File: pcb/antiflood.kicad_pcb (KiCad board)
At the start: 2 copper layers, 92 x 74 mm, 71 parts, among them J1 Barrel_Jack, J10 Screw_Terminal_01x02, J11 Screw_Terminal_01x02, J12 Screw_Terminal_01x02, J13 Screw_Terminal_01x02, J14 Screw_Terminal_01x02, J15 Screw_Terminal_01x02, J16 GS2, J2 Conn_01x04, J4 Conn_02x04_Odd_Even, J5 01x03, J7 01x03, J8 Conn_02x03_Odd_Even, J9 Conn_01x07, K1 P-5, K2 P-5, Q1 2N3904, Q2 2N3904, SW1 SW_Push, SW2 SW_Push, SW3 SW_Push, U1 ATMEGA328P-AU, U2 LM7812_TO220, U3 LM7805_TO220, U4 LM1117-3.3, Y1 16MHz

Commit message: Update.
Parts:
- removed ? (x4): MountingHole_2.5mm_Pad, Mounting_Holes:MountingHole_2.5mm_Pad
- removed J14, J15: Screw_Terminal_01x02, Connectors_Terminal_Blocks:TerminalBlock_bornier-2_P5.08mm
- removed J16: GS2, Connectors:GS2
- removed JP1: Jumper_NC_Dual, Pin_Headers:Pin_Header_Straight_1x03_Pitch2.54mm
- added C11: 22p, Capacitors_SMD:C_1206, F.Cu at (134.0, 95.9)
- added C12: 22p, Capacitors_SMD:C_1206, F.Cu at (153.0, 95.9)
- added D10: LED, LEDs:LED_1206, F.Cu at (159.4, 92.1)
- added D11: LED, LEDs:LED_1206, F.Cu at (159.4, 97.2)
- added D12: LED, LEDs:LED_1206, F.Cu at (159.4, 99.7)
- added D9: LED, LEDs:LED_1206, F.Cu at (159.4, 94.6)
- added J3: 01x03, Connectors_Terminal_Blocks:TerminalBlock_bornier-3_P5.08mm, F.Cu at (170.8, 90.8)
- added J6: Conn_02x05_Odd_Even, Socket_Strips:Socket_Strip_Straight_2x05_Pitch2.54mm, F.Cu at (132.7, 109.9)
- added L1: 170, Inductors_SMD:L_12x12mm_h6mm, F.Cu at (112.4, 79.4)
- added L2: 220, Inductors_SMD:L_12x12mm_h6mm, F.Cu at (112.4, 93.3)
- added R23: 3k3, Resistors_SMD:R_0805, F.Cu at (145.4, 112.4)
- added R24: 3k3, Resistors_SMD:R_0805, F.Cu at (145.4, 104.8)
- added R25: 3k3, Resistors_SMD:R_0805, F.Cu at (141.6, 112.4)
- added R26: 1k, Resistors_SMD:R_0805, F.Cu at (141.6, 108.6)
- added R27: 1k, Resistors_SMD:R_0805, F.Cu at (141.6, 104.8)
- added R28: 1k, Resistors_SMD:R_0805, F.Cu at (137.8, 112.4)
- added R29: 1k, Resistors_SMD:R_0805, F.Cu at (137.8, 104.8)
- added R30: 1k, Resistors_SMD:R_0805, F.Cu at (137.8, 108.6)
- added R31: 1k, Resistors_SMD:R_0805, F.Cu at (153.0, 102.2)
- added R32: 1M, Resistors_SMD:R_0805, F.Cu at (149.2, 102.2)
- added U5: MC34063, SMD_Packages:SOIC-8-N, F.Cu at (113.7, 114.9)
- added U6: TP4056, SMD_Packages:SOIC-8-N, F.Cu at (101.0, 114.9)
- C1, C5: value 0.1 -> 100; footprint Capacitors_SMD:C_1206 -> Capacitors_SMD:CP_Elec_6.3x5.7
- C10: value 22p -> 0.1
- C2, C4: value 100 -> 0.1; footprint Capacitors_SMD:CP_Elec_6.3x5.7 -> Capacitors_SMD:C_1206
- C3: value 47 -> 470
- C6: value 47 -> 0.1; footprint Capacitors_SMD:CP_Elec_6.3x5.7 -> Capacitors_SMD:C_1206
- C7: value 0.1 -> 470p
- C8: value 0.1 -> 1n5
- C9: value 22p -> 100; footprint Capacitors_SMD:C_1206 -> Capacitors_SMD:CP_Elec_6.3x5.7
- D5, D6: value LED -> D; footprint LEDs:LED_1206 -> Diodes_SMD:D_SMA
- J2: value Conn_01x04 -> 01x03; footprint Socket_Strips:Socket_Strip_Straight_1x04_Pitch2.54mm -> Connectors_Terminal_Blocks:TerminalBlock_bornier-3_P5.08mm
- J4: value Conn_02x04_Odd_Even -> Conn_02x05_Odd_Even; footprint Socket_Strips:Socket_Strip_Straight_2x04_Pitch2.54mm -> Socket_Strips:Socket_Strip_Straight_2x05_Pitch2.54mm
- J5: value 01x03 -> Conn_02x04_Odd_Even; footprint Connectors_Terminal_Blocks:TerminalBlock_bornier-3_P5.08mm -> Socket_Strips:Socket_Strip_Straight_2x04_Pitch2.54mm
- J7: value 01x03 -> Conn_02x03_Odd_Even; footprint Connectors_Terminal_Blocks:TerminalBlock_bornier-3_P5.08mm -> Socket_Strips:Socket_Strip_Straight_2x03_Pitch2.54mm
- J8: value Conn_02x03_Odd_Even -> Screw_Terminal_01x02; footprint Pin_Headers:Pin_Header_Straight_2x03_Pitch2.54mm -> Connectors_Terminal_Blocks:TerminalBlock_bornier-2_P5.08mm
- J9: value Conn_01x07 -> Screw_Terminal_01x02; footprint Socket_Strips:Socket_Strip_Straight_1x07_Pitch2.54mm -> Connectors_Terminal_Blocks:TerminalBlock_bornier-2_P5.08mm
- R1: value 82 -> 1k5
- R10: value 33k -> 1k2
- R11: value 33k -> 180
- R12: value 3k3 -> 3k6
- R13: value 0.5 -> 3k6; footprint Resistors_SMD:R_2010 -> Resistors_SMD:R_0805
- R15: value 3k3 -> 0.5; footprint Resistors_SMD:R_0805 -> Resistors_SMD:R_2010
- R16: value 1M -> R
- R17: value 100 -> 10k
- R18: value 100 -> R
- R19, R22: value 100 -> 1k5
- R20, R21: value 100 -> 3k3
- R4: value 1k5 -> 82
- R5: value 3k3 -> 1k
- R6: value 3k3 -> 0.22
- R7: value 3k3 -> 0.33
- R8: value 1k5 -> 1k
- R9: value 3k3 -> 1k2
- SW1, SW2, SW3: footprint Buttons_Switches_THT:SW_Tactile_SPST_Angled_PTS645Vx83-2LFS -> Buttons_Switches_SMD:SW_SPST_SKQG
- U1: value ATMEGA328P-AU -> LM1117-3.3; footprint Housings_QFP:TQFP-32_7x7mm_Pitch0.8mm -> TO_SOT_Packages_SMD:SOT-223-3_TabPin2
- U2: value LM7812_TO220 -> ATMEGA328P-AU; footprint TO_SOT_Packages_THT:TO-220-3_Horizontal -> Housings_QFP:TQFP-32_7x7mm_Pitch0.8mm
- U4: value LM1117-3.3 -> MC34063; footprint TO_SOT_Packages_SMD:SOT-223-3_TabPin2 -> SMD_Packages:SOIC-8-N
- moved J13 116.9 mm to (236.9, 121.3)
- moved J12 100.7 mm to (226.7, 121.3)
- moved J11 86.2 mm to (216.5, 121.3)
- moved D6 85.2 mm to (98.4, 101.0), turned to 0 degrees
- moved D5 84.1 mm to (98.4, 95.9), turned to 0 degrees
- moved SW2 80.3 mm to (197.5, 80.6), turned to 0 degrees
- moved J10 74.5 mm to (206.4, 121.3)
- moved R12 69.5 mm to (164.5, 106.0), turned to 0 degrees
- moved R7 68.5 mm to (156.8, 117.5), turned to 0 degrees
- moved U1 67.4 mm to (108.6, 106.0)
- moved R6 64.5 mm to (156.8, 113.7), turned to 0 degrees
- moved R9 62.5 mm to (160.7, 106.0), turned to 0 degrees
- moved C9 60.5 mm to (99.7, 76.8)
- moved D1 59.5 mm to (98.4, 90.8)
- moved R5 57.9 mm to (156.8, 106.0)
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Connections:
- C1 pad 1: Net-(C1-Pad1) -> +12V
- C10 pad 1: /O2 -> /RST
- C2 pad 1: Net-(C1-Pad1) -> +12V
- C3 pad 1: +12V -> +5V
- C5 pad 1: GND -> +3V3
- C5 pad 2: +5V -> GND
- C7 pad 1: +3V3 -> Net-(C7-Pad1)
- C8 pad 1: /RST -> Net-(C8-Pad1)
- C9 pad 1: /O1 -> /BAT
- D1 pad 2: /FON -> Net-(D1-Pad2)
- D2 pad 2: /FCL -> Net-(D2-Pad2)
- D4 pad 1: Net-(D3-Pad1) -> Net-(D4-Pad1)
- D5 pad 1: Net-(D3-Pad1) -> +12V
- D6 pad 1: Net-(D3-Pad1) -> Net-(D6-Pad1)
- D6 pad 2: Net-(D6-Pad2) -> GND
- D7 pad 1: Net-(D3-Pad1) -> GND
- D8 pad 1: Net-(D3-Pad1) -> GND
- J1 pad 1: Net-(C1-Pad1) -> +12V
- J10 pad 2: /A0 -> /A2
- J11 pad 2: /A1 -> /A3
- J12 pad 2: /A2 -> /A4
- J13 pad 2: /A3 -> /A5
- J2 pad 1: GND -> Net-(J2-Pad1)
- J2 pad 2: +5V -> /A6
- J4 pad 2: /WRX -> GND
- J4 pad 3: Net-(J4-Pad3) -> /BAT
- J4 pad 4: Net-(J4-Pad4) -> /BTMP
- J4 pad 5: Net-(J4-Pad5) -> /BAT
- J4 pad 6: Net-(J4-Pad6) -> /BTMP
- J4 pad 7: Net-(J4-Pad7) -> +12V
- J4 pad 8: +3V3 -> +5V
- J5 pad 1: Net-(J5-Pad1) -> GND
- J5 pad 2: /A6 -> /WRX
- J7 pad 1: Net-(J7-Pad1) -> /L4
- J7 pad 2: /A6 -> +5V
- J7 pad 3: Net-(J7-Pad3) -> /L5
- J8 pad 2: /RST -> /A0
- J9 pad 2: /L5 -> /A1
- K1 pad 10: /FON -> Net-(D1-Pad2)
- K1 pad 3: Net-(J5-Pad1) -> Net-(J2-Pad1)
- K1 pad 4: VDDA -> +12V
- K1 pad 7: VDDA -> +12V
- K1 pad 8: Net-(J7-Pad1) -> Net-(J3-Pad1)
- K2 pad 10: /FCL -> Net-(D2-Pad2)
- K2 pad 3: Net-(J5-Pad3) -> Net-(J2-Pad3)
- K2 pad 4: VDDA -> +12V
- K2 pad 7: VDDA -> +12V
- K2 pad 8: Net-(J7-Pad3) -> Net-(J3-Pad3)
- Q1 pad 3: /FON -> Net-(D1-Pad2)
- Q2 pad 3: /FCL -> Net-(D2-Pad2)
- R1 pad 1: Net-(R1-Pad1) -> Net-(D1-Pad2)
- R1 pad 2: Net-(Q1-Pad2) -> /FON
- R10 pad 1: /FON -> Net-(R10-Pad1)
- R10 pad 2: /A7 -> GND
- R11 pad 1: /A7 -> Net-(L1-Pad1)
- R11 pad 2: /FCL -> Net-(R11-Pad2)
- R12 pad 1: Net-(J4-Pad7) -> +5V
- R12 pad 2: GND -> Net-(R12-Pad2)
- R13 pad 1: GND -> +12V
- R13 pad 2: /A6 -> Net-(R10-Pad1)
- R14 pad 1: GND -> /A6
- R14 pad 2: /A6 -> GND
- R15 pad 1: +5V -> /A6
- R15 pad 2: /RST -> GND
- R16 pad 1: /O1 -> /BTMP
- R16 pad 2: /O2 -> +5V
- R17 pad 1: Net-(D3-Pad2) -> Net-(R17-Pad1)
- R17 pad 2: /L0 -> GND
- R18 pad 1: Net-(D4-Pad2) -> /BTMP
- R18 pad 2: /L1 -> GND
- R19 pad 1: Net-(D5-Pad2) -> Net-(J5-Pad4)
- R19 pad 2: /L2 -> /WCC
- R2 pad 1: Net-(R2-Pad1) -> /PON
- R2 pad 2: Net-(Q2-Pad2) -> Net-(Q1-Pad2)
- R20 pad 1: Net-(D6-Pad2) -> Net-(J5-Pad4)
- R20 pad 2: /L3 -> GND
- R21 pad 1: Net-(D7-Pad2) -> Net-(J5-Pad5)
- R21 pad 2: /L4 -> +3V3
- R22 pad 1: Net-(D8-Pad2) -> Net-(J5-Pad7)
- R22 pad 2: /L5 -> /WTX
- R3 pad 1: Net-(J4-Pad4) -> Net-(D2-Pad2)
- R3 pad 2: /WCE -> /FCL
- R4 pad 1: Net-(J4-Pad6) -> Net-(Q2-Pad2)
- R4 pad 2: /WCR -> /PCL
- R5 pad 1: GND -> +5V
- R5 pad 2: Net-(J4-Pad4) -> Net-(D3-Pad2)
- R6 pad 1: Net-(J4-Pad6) -> Net-(L1-Pad1)
- R6 pad 2: GND -> /BAT
- R7 pad 1: Net-(J4-Pad5) -> Net-(R7-Pad1)
- R7 pad 2: +3V3 -> +12V
- R8 pad 1: Net-(J4-Pad7) -> +5V
- R8 pad 2: /WTX -> Net-(D4-Pad2)
- R9 pad 1: Net-(J4-Pad3) -> Net-(R12-Pad2)
- R9 pad 2: +3V3 -> GND
- SW1 pad 1: /FON -> Net-(D1-Pad2)
- SW2 pad 1: /FCL -> Net-(D2-Pad2)
- U1 pad 1: /WCR -> GND
- U1 pad 2: Net-(J2-Pad4) -> +5V
- U1 pad 3: GND -> +12V
- U2 pad 1: Net-(C1-Pad1) -> /CHG
- U2 pad 2: GND -> /FON
- U2 pad 3: +12V -> GND
- U3 pad 1: +12V -> +5V
- U3 pad 3: +5V -> +3V3
- U4 pad 1: GND -> Net-(R7-Pad1)
- U4 pad 2: +3V3 -> Net-(D6-Pad1)
- U4 pad 3: +5V -> Net-(C7-Pad1)
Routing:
- net +5V: track 224.7 -> 0.00 mm, vias 5 -> 0
- net GND: track 180.6 -> 0.00 mm, vias 23 -> 0
- net /A6: track 132.7 -> 0.00 mm, vias 2 -> 0
- net /A7: track 113.2 -> 0.00 mm, vias 3 -> 0
- net /WRX: track 67.3 -> 0.00 mm, vias 2 -> 0
- net +12V: track 65.7 -> 0.00 mm
- net /L5: track 64.0 -> 0.00 mm
- net /A5: track 61.9 -> 0.00 mm
- net /WCE: track 59.9 -> 0.00 mm
- net /L3: track 58.1 -> 0.00 mm
- net /L4: track 56.6 -> 0.00 mm
- net /WTX: track 55.7 -> 0.00 mm
- net VDDA: track 55.2 -> 0.00 mm
- net +3V3: track 54.2 -> 0.00 mm
- net /RST: track 54.1 -> 0.00 mm, vias 1 -> 0
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- removed copper zone on B.Cu, net GND
- removed copper zone on F.Cu, net GND
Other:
- board outline removed
- board text removed: "12V"
- board text removed: "5V"
- board text removed: "ANTIFLOOD PROJECT BETA 174:DBAC3ABEB3F1"
- board text removed: "Copyright 17 sep 2018 Alexey <Inverse> Shumeiko"
- board text removed: "ESP01"
- board text removed: "ICSP"
- board text removed: "Valve Control Module"
- board text removed: "dbg"
- board text removed: "λ"

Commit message: PCB: add borders
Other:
- board outline added: 88 x 84 mm
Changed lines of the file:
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@@
     (links 207)
     (no_connects 207)
-    (area 0 0 0 0)
+    (area 94.699999 62.74 248.023573 136.12)
     (thickness 1.6)
-    (drawings 0)
+    (drawings 21)
     (tracks 0)
     (zones 0)
@@
   (layers
     (0 F.Cu signal)
-    (31 B.Cu signal hide)
+    (31 B.Cu signal)
     (32 B.Adhes user)
     (33 F.Adhes user)
@@
     (pad_drill 1.3)
     (pad_to_mask_clearance 0)
-    (aux_axis_origin 103.505 53.975)
-    (grid_origin 103.505 53.975)
-    (visible_elements FFFEF77F)
+    (aux_axis_origin 71.505 50.975)
+    (grid_origin 71.505 50.975)
+    (visible_elements FFFE317F)
     (pcbplotparams
       (layerselection 0x00030_80000001)
@@
     )
   )
+  (gr_line (start 158.505 57.975) (end 72.505 57.975) (angle 90) (layer Eco1.User) (width 0.2))
+  (gr_line (start 158.505 127.975) (end 72.505 127.975) (angle 90) (layer Eco1.User) (width 0.2))
+  (gr_line (start 76.505 67.975) (end 80.505 67.975) (angle 90) (layer Eco2.User) (width 0.2))
+  (gr_line (start 78.505 69.975) (end 78.505 65.975) (angle 90) (layer Eco2.User) (width 0.2))
+  (gr_line (start 76.505 117.975) (end 80.505 117.975) (angle 90) (layer Eco2.User) (width 0.2))
+  (gr_line (start 78.505 115.975) (end 78.505 119.975) (angle 90) (layer Eco2.User) (width 0.2))
+  (gr_line (start 153.505 67.975) (end 149.505 67.975) (angle 90) (layer Eco2.User) (width 0.2))
+  (gr_line (start 151.505 69.975) (end 151.505 65.975) (angle 90) (layer Eco2.User) (width 0.2))
+  (gr_line (start 151.505 115.975) (end 151.505 119.975) (angle 90) (layer Eco2.User) (width 0.2))
+  (gr_line (start 149.505 117.975) (end 153.505 117.975) (angle 90) (layer Eco2.User) (width 0.2))
+  (gr_line (start 105.505 136.975) (end 105.505 135.975) (angle 90) (layer Eco1.User) (width 0.2))
+  (gr_line (start 105.505 112.975) (end 105.505 135.975) (angle 90) (layer Eco1.User) (width 0.2))
+  (gr_line (start 125.505 112.975) (end 125.505 136.975) (angle 90) (layer Eco1.User) (width 0.2))
+  (gr_line (start 161.505 112.975) (end 69.505 112.975) (angle 90) (layer Eco1.User) (width 0.2))
+  (gr_line (start 69.505 72.975) (end 161.505 72.975) (angle 90) (layer Eco1.User) (width 0.2))
+  (gr_line (start 115.505 48.975) (end 115.505 136.975) (angle 90) (layer Eco2.User) (width 0.2))
+  (gr_line (start 69.505 92.975) (end 161.505 92.975) (angle 90) (layer Eco2.User) (width 0.2))
+  (gr_line (start 71.505 134.975) (end 71.505 50.975) (angle 90) (layer Edge.Cuts) (width 0.1))
+  (gr_line (start 159.505 134.975) (end 71.505 134.975) (angle 90) (layer Edge.Cuts) (width 0.1))
+  (gr_line (start 159.505 50.975) (end 159.505 134.975) (angle 90) (layer Edge.Cuts) (width 0.1))
+  (gr_line (start 71.505 50.975) (end 159.505 50.975) (angle 90) (layer Edge.Cuts) (width 0.1))
 )

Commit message: PCB: pre placement of lements
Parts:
- moved J8 130.0 mm to (74.3, 55.0)
- moved J9 129.7 mm to (84.8, 55.0)
- moved J10 129.4 mm to (95.3, 55.0)
- moved J11 129.1 mm to (105.8, 55.0)
- moved J12 128.8 mm to (116.3, 55.0)
- moved J13 128.5 mm to (126.8, 55.0)
- moved SW1 123.5 mm to (76.1, 131.5)
- moved SW2 117.0 mm to (92.1, 131.5)
- moved SW3 117.0 mm to (101.0, 131.5)
- moved D11 85.0 mm to (81.7, 131.5), turned to 90 degrees
- moved D12 81.6 mm to (84.2, 131.5), turned to 90 degrees
- moved C12 74.7 mm to (83.7, 123.6), turned to 90 degrees
- moved J5 64.3 mm to (76.3, 83.2), turned to 90 degrees
- moved R1 58.2 mm to (209.0, 101.5)
- moved R10 58.2 mm to (216.7, 93.9)
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
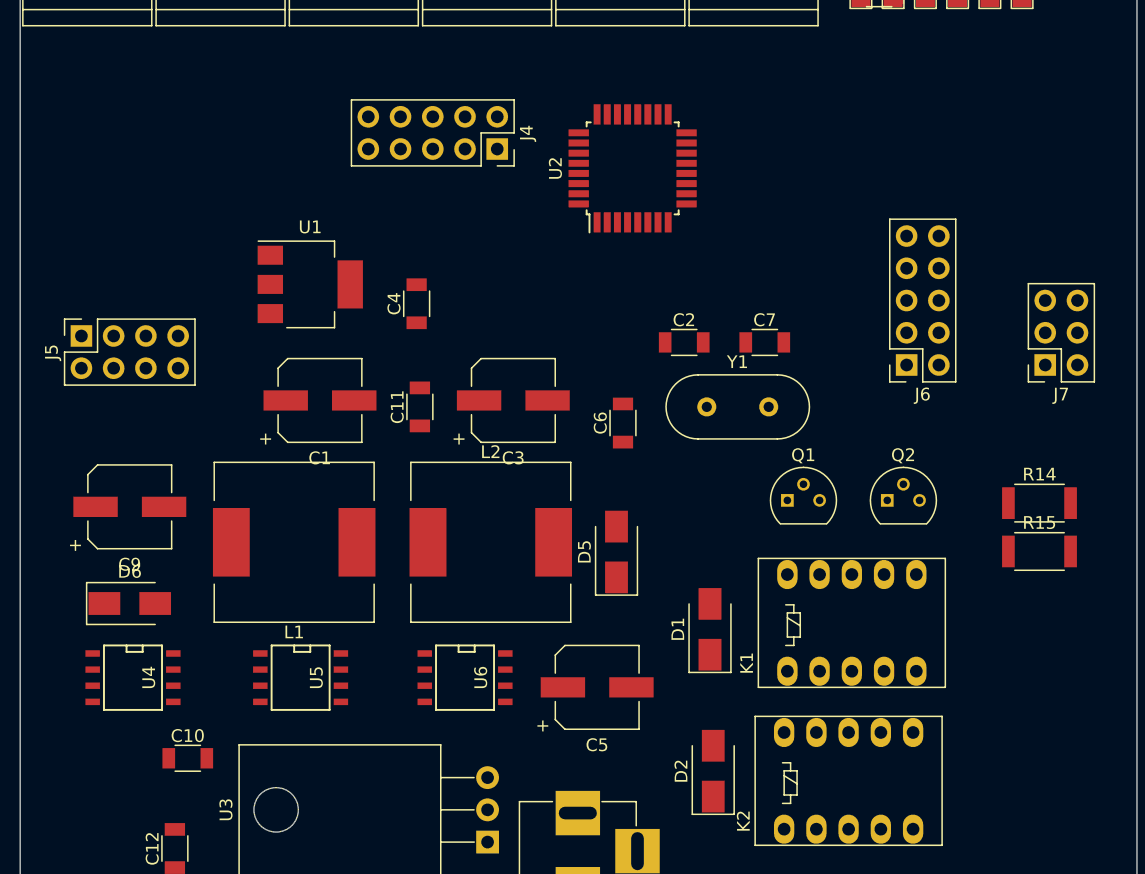
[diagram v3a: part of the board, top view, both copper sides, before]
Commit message: Schematics: rework power lines
1. Replace MC34063 with MT3608, which has a plain EN-pin.
2. Automatic controls on booster and charger.
3. CPU awarness about external power presence.
4. CPU awarness of battery voltage.
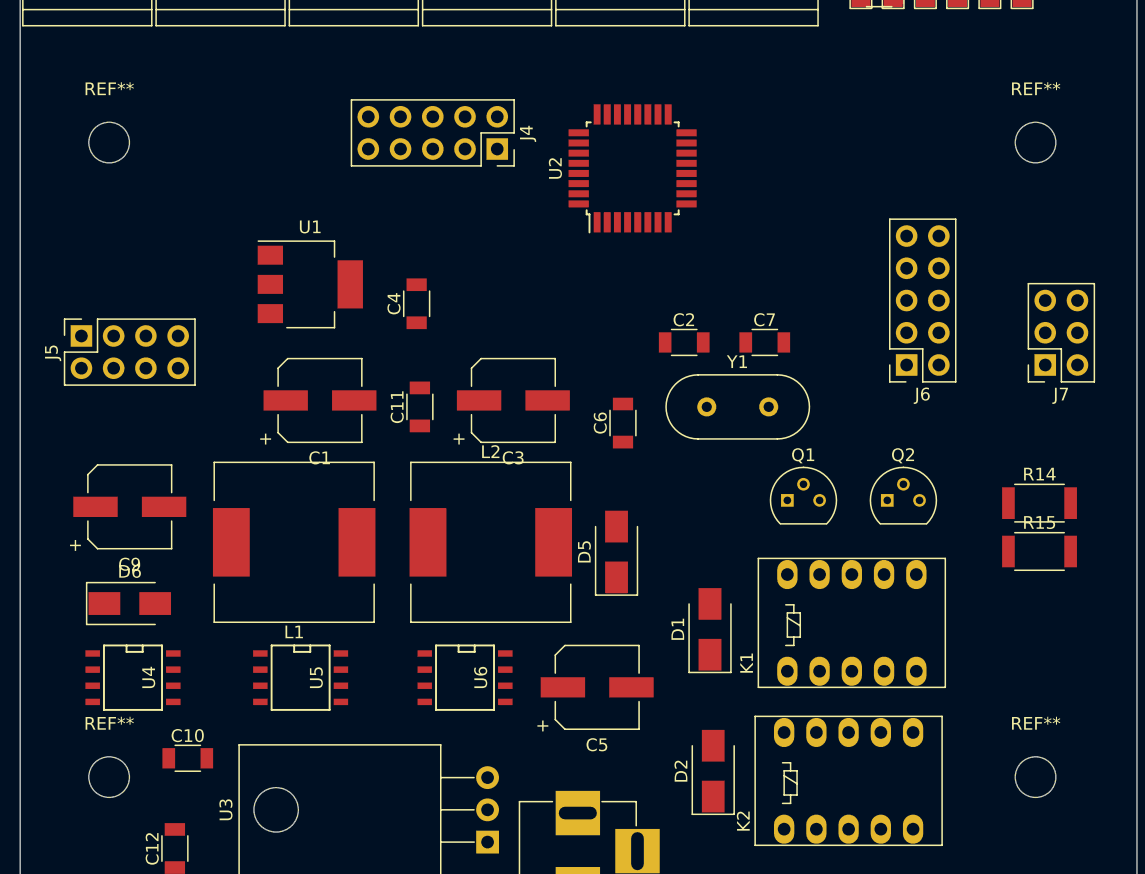
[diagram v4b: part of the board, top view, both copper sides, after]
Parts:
- added REF**: MountingHole_3.2mm_M3, Mounting_Holes:MountingHole_3.2mm_M3, F.Cu at (151.5, 118.0)
- added REF**: MountingHole_3.2mm_M3, Mounting_Holes:MountingHole_3.2mm_M3, F.Cu at (78.5, 118.0)
- added REF**: MountingHole_3.2mm_M3, Mounting_Holes:MountingHole_3.2mm_M3, F.Cu at (78.5, 68.0)
- added REF**: MountingHole_3.2mm_M3, Mounting_Holes:MountingHole_3.2mm_M3, F.Cu at (151.5, 68.0)
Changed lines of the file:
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@@
     (links 207)
     (no_connects 207)
-    (area 71.454999 50.924999 159.555001 135.025001)
+    (area 2.046999 48.874999 222.240001 137.075001)
     (thickness 1.6)
     (drawings 21)
     (tracks 0)
     (zones 0)
-    (modules 85)
+    (modules 89)
     (nets 64)
   )
@@
     (add_net "Net-(R7-Pad1)")
   )
+  (module Mounting_Holes:MountingHole_3.2mm_M3 (layer F.Cu)
+    (at 151.515 117.993)
+    (descr "Mounting Hole 3.2mm, no annular, M3")
+    (tags "mounting hole 3.2mm no annular m3")
+    (attr virtual)
+    (fp_text reference REF** (at 0 -4.2) (layer F.SilkS)
+      (effects (font (size 1 1) (thickness 0.15)))
+    )
+    (fp_text value MountingHole_3.2mm_M3 (at 0 4.2) (layer F.Fab)
+      (effects (font (size 1 1) (thickness 0.15)))
+    )
+    (fp_text user %R (at 0.3 0) (layer F.Fab)
+      (effects (font (size 1 1) (thickness 0.15)))
+    )
+    (fp_circle (center 0 0) (end 3.2 0) (layer Cmts.User) (width 0.15))
+    (fp_circle (center 0 0) (end 3.45 0) (layer F.CrtYd) (width 0.05))
+    (pad 1 np_thru_hole circle (at 0 0) (size 3.2 3.2) (drill 3.2) (layers *.Cu *.Mask))
+  )
+  (module Mounting_Holes:MountingHole_3.2mm_M3 (layer F.Cu)
+    (at 78.515 117.993)
+    (descr "Mounting Hole 3.2mm, no annular, M3")
+    (tags "mounting hole 3.2mm no annular m3")
+    (attr virtual)
+    (fp_text reference REF** (at 0 -4.2) (layer F.SilkS)
+      (effects (font (size 1 1) (thickness 0.15)))
+    )
+    (fp_text value MountingHole_3.2mm_M3 (at 0 4.2) (layer F.Fab)
+      (effects (font (size 1 1) (thickness 0.15)))
+    )
+    (fp_text user %R (at 0.3 0) (layer F.Fab)
+      (effects (font (size 1 1) (thickness 0.15)))
+    )
+    (fp_circle (center 0 0) (end 3.2 0) (layer Cmts.User) (width 0.15))
+    (fp_circle (center 0 0) (end 3.45 0) (layer F.CrtYd) (width 0.05))
+    (pad 1 np_thru_hole circle (at 0 0) (size 3.2 3.2) (drill 3.2) (layers *.Cu *.Mask))
+  )
+  (module Mounting_Holes:MountingHole_3.2mm_M3 (layer F.Cu)
+    (at 78.515 67.993)
+    (descr "Mounting Hole 3.2mm, no annular, M3")
+    (tags "mounting hole 3.2mm no annular m3")
+    (attr virtual)
+    (fp_text reference REF** (at 0 -4.2) (layer F.SilkS)
+      (effects (font (size 1 1) (thickness 0.15)))
+    )
+    (fp_text value MountingHole_3.2mm_M3 (at 0 4.2) (layer F.Fab)
+      (effects (font (size 1 1) (thickness 0.15)))
+    )
+    (fp_text user %R (at 0.3 0) (layer F.Fab)
+      (effects (font (size 1 1) (thickness 0.15)))
+    )
+    (fp_circle (center 0 0) (end 3.2 0) (layer Cmts.User) (width 0.15))
+    (fp_circle (center 0 0) (end 3.45 0) (layer F.CrtYd) (width 0.05))
+    (pad 1 np_thru_hole circle (at 0 0) (size 3.2 3.2) (drill 3.2) (layers *.Cu *.Mask))
+  )
+  (module Mounting_Holes:MountingHole_3.2mm_M3 (layer F.Cu)
+    (at 151.515 67.993)
+    (descr "Mounting Hole 3.2mm, no annular, M3")
+    (tags "mounting hole 3.2mm no annular m3")
+    (attr virtual)
+    (fp_text reference REF** (at 0 -4.2) (layer F.SilkS)
+      (effects (font (size 1 1) (thickness 0.15)))
+    )
+    (fp_text value MountingHole_3.2mm_M3 (at 0 4.2) (layer F.Fab)
+      (effects (font (size 1 1) (thickness 0.15)))
+    )
+    (fp_text user %R (at 0.3 0) (layer F.Fab)
+      (effects (font (size 1 1) (thickness 0.15)))
+    )
+    (fp_circle (center 0 0) (end 3.2 0) (layer Cmts.User) (width 0.15))
+    (fp_circle (center 0 0) (end 3.45 0) (layer F.CrtYd) (width 0.05))
+    (pad 1 np_thru_hole circle (at 0 0) (size 3.2 3.2) (drill 3.2) (layers *.Cu *.Mask))
+  )
   (module Capacitors_SMD:CP_Elec_6.3x5.7 (layer F.Cu)
